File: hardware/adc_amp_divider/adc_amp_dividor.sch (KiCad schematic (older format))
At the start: 95 parts, among them M1 CONN_1, M2 CONN_1, M3 CONN_1, P1 CONN_10X2, P2 CONN_4, P3 CONN_6, P4 CONN_3, U1 LMV324IDR, U2 LMV324IDR, U3 LMV324IDR

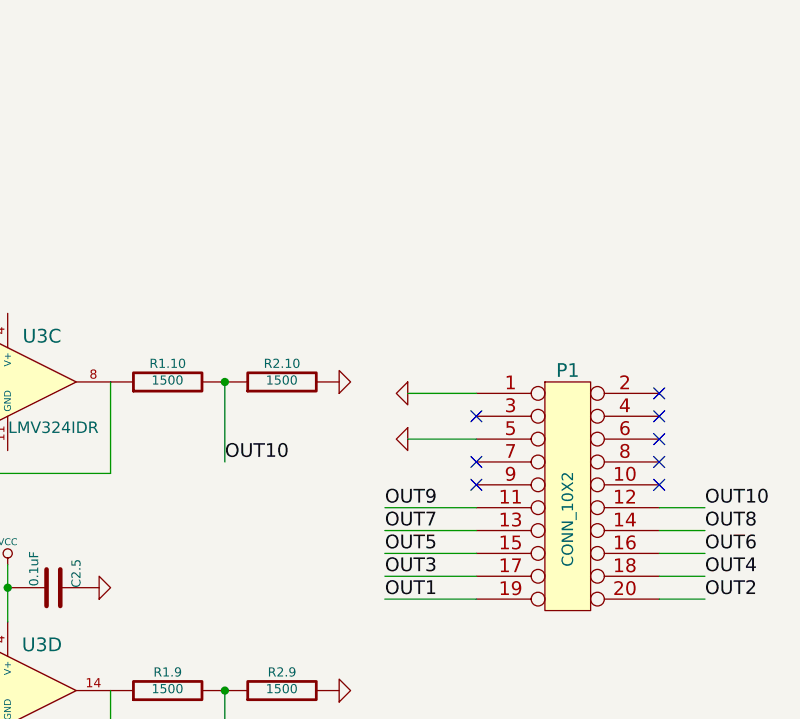
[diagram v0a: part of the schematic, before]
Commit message: PA5 is now free
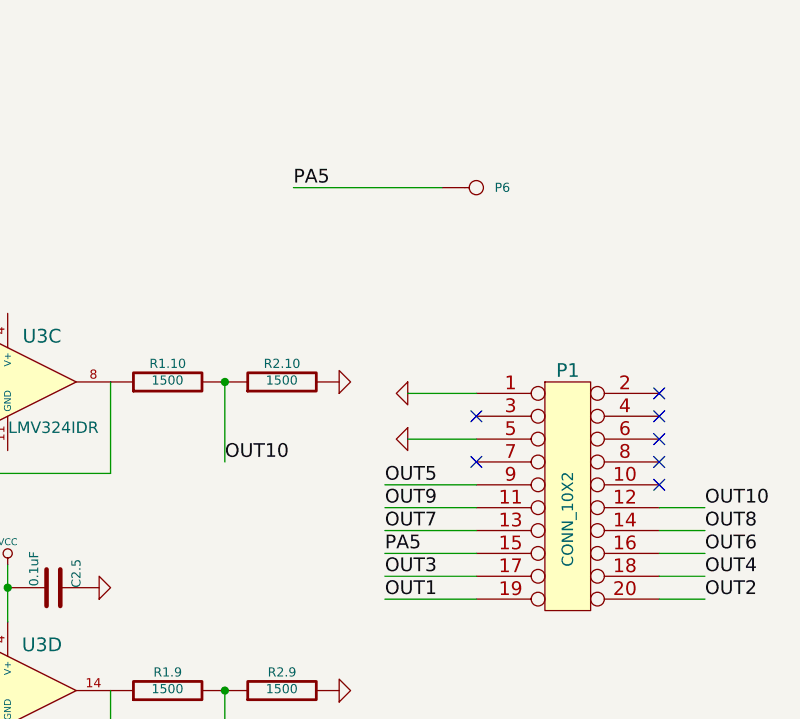
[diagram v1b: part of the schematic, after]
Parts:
- added P6: CONN_1, symbol CONN_1
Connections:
- net labels added: PA5
- wire segments 126 -> 128
- no-connect marks 11 -> 10
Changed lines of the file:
@@
 Text Label 1700 8600 0    60   ~ 0
 INP1
-NoConn ~ 15050 7850
 NoConn ~ 15050 7550
 NoConn ~ 15850 7450
@@
 Text Label 16050 8150 0    60   ~ 0
 OUT6
-Text Label 14650 8150 0    60   ~ 0
+Text Label 14650 7850 0    60   ~ 0
 OUT5
 Text Label 14650 8050 0    60   ~ 0
@@
 $EndComp
 NoConn ~ 15800 3100
+$Comp
+L CONN_1 P6
+U 1 1 52941801
+P 15050 6550
+F 0 "P6" H 15130 6550 40  0000 L CNN
+F 1 "CONN_1" H 15050 6605 30  0001 C CNN
+F 2 "" H 15050 6550 60  0000 C CNN
+F 3 "" H 15050 6550 60  0000 C CNN
+	1    15050 6550
+	1    0    0    -1
+$EndComp
+Wire Wire Line
+	14250 6550 14900 6550
+Text Label 14250 6550 0    60   ~ 0
+PA5
+Wire Wire Line
+	14650 7850 15050 7850
+Text Label 14650 8150 0    60   ~ 0
+PA5
 $EndSCHEMATC

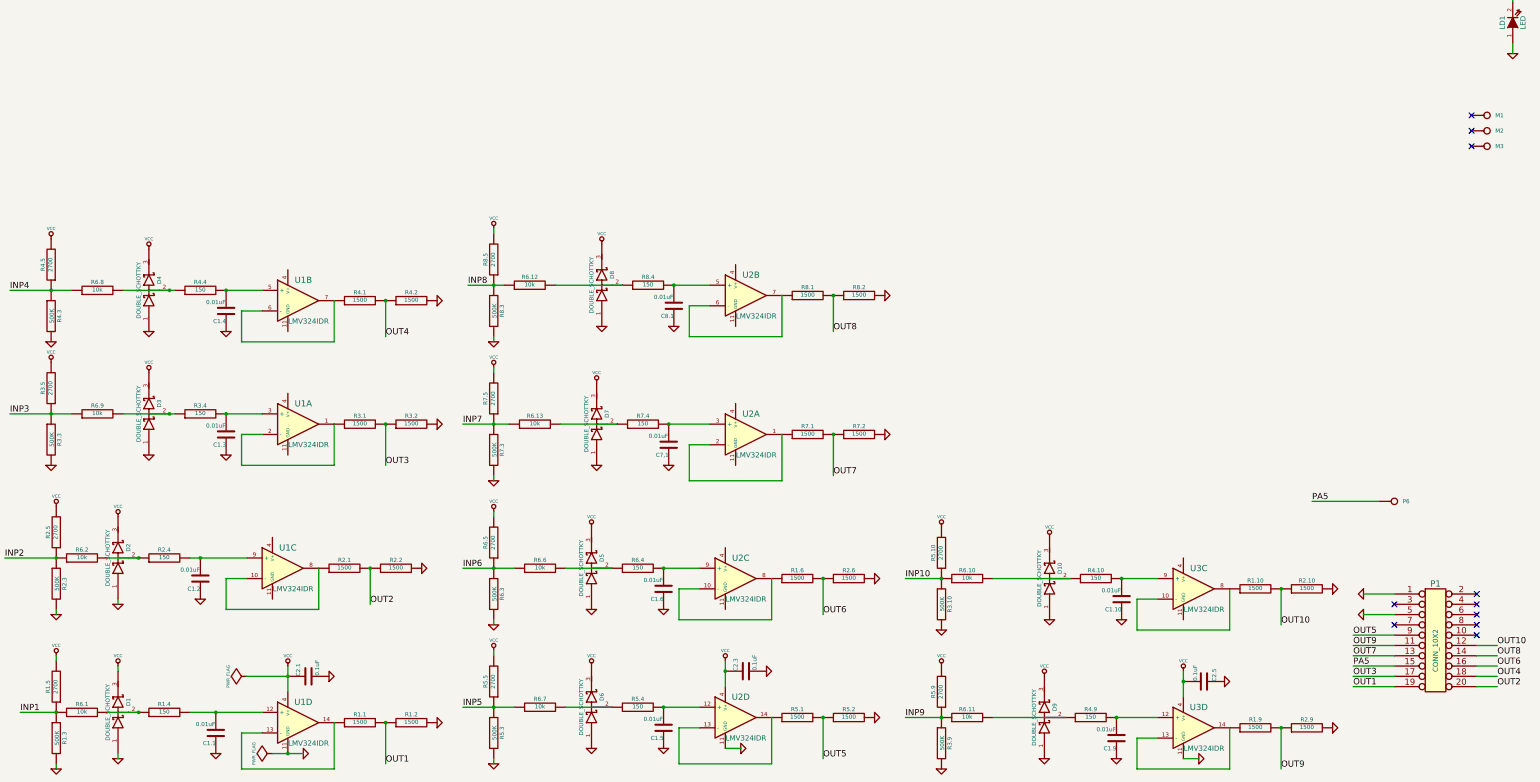
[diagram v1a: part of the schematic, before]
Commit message: now 12 channels
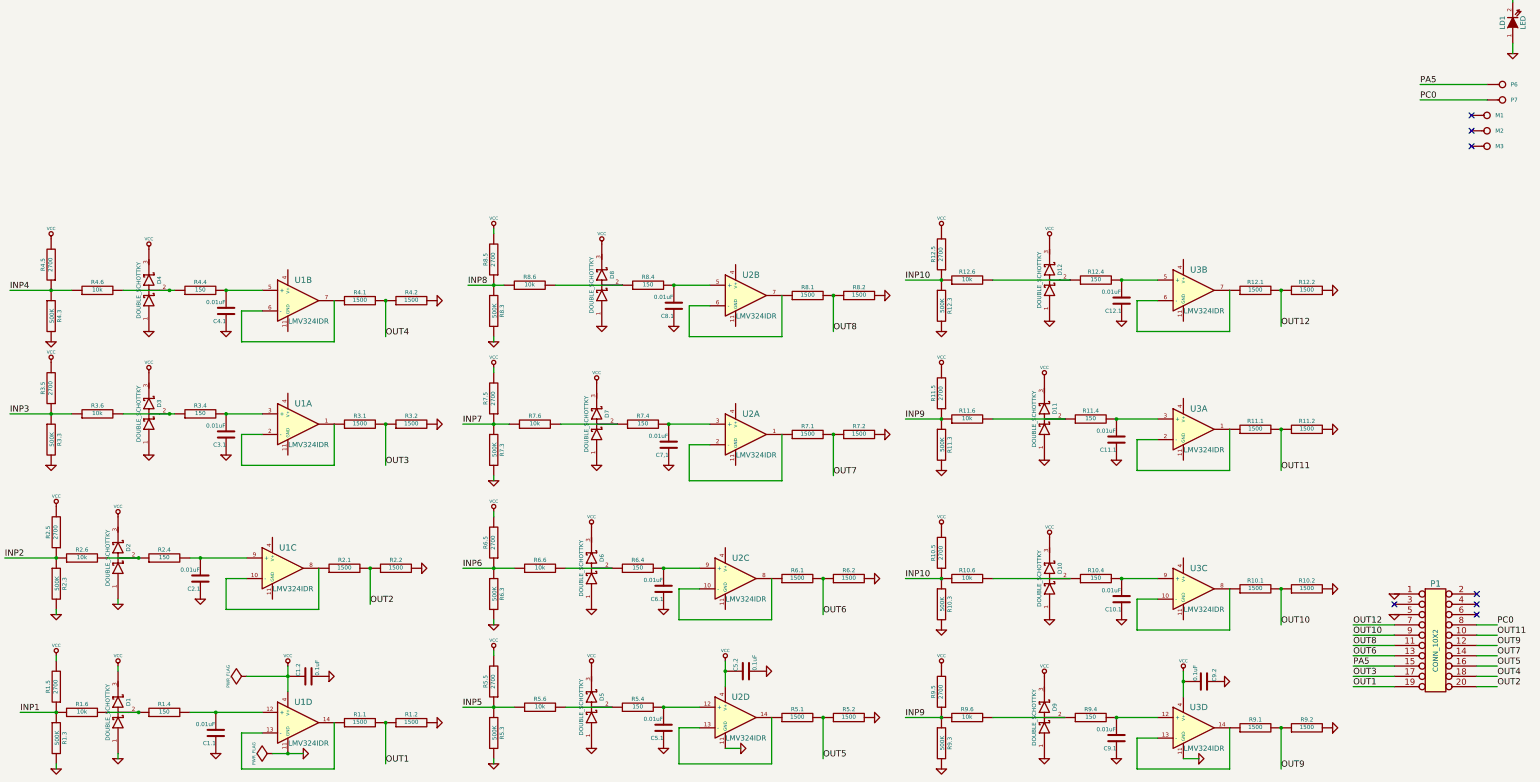
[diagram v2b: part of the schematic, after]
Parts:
- added C11.1, C12.1: 0.01uF, ~, symbol C
- added D11, D12: DOUBLE_SCHOTTKY, ~, symbol DOUBLE_SCHOTTKY
- added P7: CONN_1, symbol CONN_1
- added R11.1, R11.2, R12.1, R12.2: 1500, ~, symbol R
- added R11.3, R12.3: 500K, ~, symbol R
- added R11.4, R12.4: 150, ~, symbol R
- added R11.5, R12.5: 2700, ~, symbol R
- added R11.6, R12.6: 10k, ~, symbol R
- added unit 1 of U3
- added unit 2 of U3
- renumbered C2.1 to C1.2, C1.10 to C10.1, C1.2 to C2.1, C1.3 to C3.1, C1.4 to C4.1, C1.5 to C5.1, C2.3 to C5.2, C1.6 to C6.1, C1.9 to C9.1, C2.5 to C9.2, D6 to D5, D5 to D6, R6.1 to R1.6, R1.10 to R10.1, R2.10 to R10.2, R3.10 to R10.3, R4.10 to R10.4, R5.10 to R10.5, R6.10 to R10.6, R6.2 to R2.6, R6.9 to R3.6, R6.8 to R4.6, R6.7 to R5.6, R1.6 to R6.1, R2.6 to R6.2, R6.13 to R7.6, R6.12 to R8.6, R1.9 to R9.1, R2.9 to R9.2, R3.9 to R9.3, R4.9 to R9.4, R5.9 to R9.5, R6.11 to R9.6
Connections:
- net labels added: OUT11, OUT12, PC0
- wire segments 128 -> 146
- no-connect marks 10 -> 7
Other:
- moved on the sheet: P6

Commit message: my changes
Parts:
- removed P4: CONN_3, symbol CONN_3
- added P4, P8: CONN_2, symbol CONN_2
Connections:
- wire segments 146 -> 147

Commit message: fresh version
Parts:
- removed P2: CONN_4, symbol CONN_4
- removed P4, P8: CONN_2, symbol CONN_2
- added P2: CONN_6, symbol CONN_6
- added P4: CONN_3, symbol CONN_3
- added P5: CONN_2, SIL-2, symbol CONN_2
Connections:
- net labels added: INP11, INP12
- wire segments 147 -> 149
- no-connect marks 7 -> 6
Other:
- note added: "mountng screws"
- moved on the sheet: M1, M2, M3
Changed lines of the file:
@@
 INP1
 NoConn ~ 15050 7550
-NoConn ~ 15850 7450
 NoConn ~ 15850 7550
 NoConn ~ 15850 7650
@@
 Text Label 16050 8350 0    60   ~ 0
 OUT2
-$Comp
-L CONN_4 P2
-U 1 1 5234FB36
-P 700 6600
-F 0 "P2" V 650 6600 50  0000 C CNN
-F 1 "CONN_4" V 750 6600 50  0000 C CNN
-F 2 "" H 700 6600 60  0000 C CNN
-F 3 "" H 700 6600 60  0000 C CNN
-	1    700  6600
-	-1   0    0    1
-$EndComp
-Text Label 1250 6450 0    60   ~ 0
+Text Label 1250 8500 0    60   ~ 0
 INP1
-Text Label 1250 6550 0    60   ~ 0
+Text Label 1250 8400 0    60   ~ 0
 INP2
-Text Label 1250 6650 0    60   ~ 0
+Text Label 1250 8300 0    60   ~ 0
 INP3
-Text Label 1250 6750 0    60   ~ 0
+Text Label 1250 8200 0    60   ~ 0
 INP4
 $Comp
@@
 $EndComp
 $Comp
+L CONN_3 P4
+U 1 1 524F6D3B
+P 15850 900
+F 0 "P4" V 15800 900 50  0000 C CNN
+F 1 "CONN_3" V 15900 900 40  0000 C CNN
+F 2 "" H 15850 900 60  0000 C CNN
+F 3 "" H 15850 900 60  0000 C CNN
+	1    15850 900
+	-1   0    0    1
+$EndComp
+$Comp
 L VCC #PWR041
 U 1 1 524F6E51
@@
 Connection ~ 4300 8250
 Wire Wire Line
-	1050 6750 1250 6750
-Wire Wire Line
-	1050 6650 1250 6650
-Wire Wire Line
-	1050 6550 1250 6550
-Wire Wire Line
-	1050 6450 1250 6450
+	1050 8500 1250 8500
+Wire Wire Line
+	1050 8400 1250 8400
+Wire Wire Line
+	1050 8300 1250 8300
+Wire Wire Line
+	1050 8200 1250 8200
 Wire Wire Line
 	3350 8600 4050 8600
@@
 Wire Wire Line
 	15050 7950 14650 7950
+Connection ~ 16200 900
 Connection ~ 16200 800
-Text Label 1250 7550 0    60   ~ 0
+Text Label 1250 7650 0    60   ~ 0
 INP8
-Text Label 1250 7450 0    60   ~ 0
+Text Label 1250 7750 0    60   ~ 0
 INP7
-Text Label 1250 7350 0    60   ~ 0
+Text Label 1250 8000 0    60   ~ 0
 INP6
-Text Label 1250 7250 0    60   ~ 0
+Text Label 1250 8100 0    60   ~ 0
 INP5
 $Comp
@@
 F 3 "" H 700 7500 60  0000 C CNN
 	1    700  7500
-	-1   0    0    1
-$EndComp
-Text Label 1250 7650 0    60   ~ 0
+	-1   0    0    -1
+$EndComp
+Text Label 1250 7550 0    60   ~ 0
 INP9
-Text Label 1250 7750 0    60   ~ 0
+Text Label 1250 7450 0    60   ~ 0
 INP10
 Wire Wire Line
@@
 L CONN_1 M1
 U 1 1 52530AFC
-P 15950 2800
-F 0 "M1" H 16030 2800 40  0000 L CNN
-F 1 "CONN_1" H 15950 2855 30  0001 C CNN
-F 2 "" H 15950 2800 60  0000 C CNN
-F 3 "" H 15950 2800 60  0000 C CNN
-	1    15950 2800
+P 15950 3150
+F 0 "M1" H 16030 3150 40  0000 L CNN
+F 1 "CONN_1" H 15950 3205 30  0001 C CNN
+F 2 "" H 15950 3150 60  0000 C CNN
+F 3 "" H 15950 3150 60  0000 C CNN
+	1    15950 3150
 	1    0    0    -1
 $EndComp
@@
 L CONN_1 M2
 U 1 1 52530B0B
-P 15950 2950
-F 0 "M2" H 16030 2950 40  0000 L CNN
-F 1 "CONN_1" H 15950 3005 30  0001 C CNN
-F 2 "" H 15950 2950 60  0000 C CNN
-F 3 "" H 15950 2950 60  0000 C CNN
-	1    15950 2950
-	1    0    0    -1
-$EndComp
-NoConn ~ 15800 2800
-NoConn ~ 15800 2950
+P 15950 3300
+F 0 "M2" H 16030 3300 40  0000 L CNN
+F 1 "CONN_1" H 15950 3355 30  0001 C CNN
+F 2 "" H 15950 3300 60  0000 C CNN
+F 3 "" H 15950 3300 60  0000 C CNN
+	1    15950 3300
+	1    0    0    -1
+$EndComp
+NoConn ~ 15800 3150
+NoConn ~ 15800 3300
 $Comp
 L DOUBLE_SCHOTTKY D6
@@
 L CONN_1 M3
 U 1 1 52896702
-P 15950 3100
-F 0 "M3" H 16030 3100 40  0000 L CNN
-F 1 "CONN_1" H 15950 3155 30  0001 C CNN
-F 2 "" H 15950 3100 60  0000 C CNN
-F 3 "" H 15950 3100 60  0000 C CNN
-	1    15950 3100
-	1    0    0    -1
-$EndComp
-NoConn ~ 15800 3100
+P 15950 3450
+F 0 "M3" H 16030 3450 40  0000 L CNN
+F 1 "CONN_1" H 15950 3505 30  0001 C CNN
+F 2 "" H 15950 3450 60  0000 C CNN
+F 3 "" H 15950 3450 60  0000 C CNN
+	1    15950 3450
+	1    0    0    -1
+$EndComp
+NoConn ~ 15800 3450
 $Comp
 L CONN_1 P6
@@
 $EndComp
 Text Label 10300 5750 0    60   ~ 0
-INP9
+INP11
 Text Label 13950 6250 0    60   ~ 0
 OUT11
@@
 OUT12
 Text Label 10300 4400 0    60   ~ 0
-INP10
+INP12
 $Comp
 L R R11.3
@@
 PC0
 $Comp
-L CONN_2 P8
-U 1 1 5295E356
-P 15950 3600
-F 0 "P8" V 15900 3600 40  0000 C CNN
-F 1 "CONN_2" V 16000 3600 40  0000 C CNN
-F 2 "" H 15950 3600 60  0000 C CNN
-F 3 "" H 15950 3600 60  0000 C CNN
-	1    15950 3600
-	-1   0    0    1
-$EndComp
-Wire Wire Line
-	16300 3500 16300 3900
+L CONN_6 P2
+U 1 1 52967E40
+P 700 8250
+F 0 "P2" V 650 8250 60  0000 C CNN
+F 1 "CONN_6" V 750 8250 60  0000 C CNN
+F 2 "" H 700 8250 60  0000 C CNN
+F 3 "" H 700 8250 60  0000 C CNN
+	1    700  8250
+	-1   0    0    -1
+$EndComp
+Wire Wire Line
+	1050 8100 1250 8100
+Wire Wire Line
+	1050 8000 1250 8000
+Text Label 1250 7350 0    60   ~ 0
+INP11
+Text Label 1250 7250 0    60   ~ 0
+INP12
+Text Notes 15500 3600 0    60   ~ 0
+mountng screws
+Wire Notes Line
+	16350 3050 16350 3650
+Wire Notes Line
+	16350 3650 15400 3650
+Wire Notes Line
+	15400 3650 15400 3050
+Wire Notes Line
+	15400 3050 16350 3050
+$Comp
+L CONN_2 P5
+U 1 1 5296836D
+P 15350 1850
+F 0 "P5" V 15300 1850 40  0000 C CNN
+F 1 "CONN_2" V 15400 1850 40  0000 C CNN
+F 2 "SIL-2" H 15350 1850 60  0001 C CNN
+F 3 "" H 15350 1850 60  0000 C CNN
+	1    15350 1850
+	1    0    0    -1
+$EndComp
 $Comp
 L GND #PWR088
-U 1 1 5295E451
-P 16300 3900
-F 0 "#PWR088" H 16300 3900 30  0001 C CNN
-F 1 "GND" H 16300 3830 30  0001 C CNN
-F 2 "" H 16300 3900 60  0000 C CNN
-F 3 "" H 16300 3900 60  0000 C CNN
-	1    16300 3900
-	1    0    0    -1
-$EndComp
-Connection ~ 16300 3700
-$Comp
-L CONN_2 P4
-U 1 1 5295E49A
-P 15850 900
-F 0 "P4" V 15800 900 40  0000 C CNN
-F 1 "CONN_2" V 15900 900 40  0000 C CNN
-F 2 "" H 15850 900 60  0000 C CNN
-F 3 "" H 15850 900 60  0000 C CNN
-	1    15850 900
-	-1   0    0    1
-$EndComp
+U 1 1 52968557
+P 15850 7450
+F 0 "#PWR088" H 15850 7450 30  0001 C CNN
+F 1 "GND" H 15850 7380 30  0001 C CNN
+F 2 "" H 15850 7450 60  0000 C CNN
+F 3 "" H 15850 7450 60  0000 C CNN
+	1    15850 7450
+	1    0    0    -1
+$EndComp
+$Comp
+L GND #PWR089
+U 1 1 5296855D
+P 15000 1950
+F 0 "#PWR089" H 15000 1950 30  0001 C CNN
+F 1 "GND" H 15000 1880 30  0001 C CNN
+F 2 "" H 15000 1950 60  0000 C CNN
+F 3 "" H 15000 1950 60  0000 C CNN
+	1    15000 1950
+	1    0    0    -1
+$EndComp
+Wire Wire Line
+	15000 1950 15000 1750
 $EndSCHEMATC
